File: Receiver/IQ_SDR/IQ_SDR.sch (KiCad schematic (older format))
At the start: 150 parts, among them CON1 SJ1-3523N, J1 ANT, J10 LO_I, J11 LO_Q, J12 GNDA, J13 I_IN, J14 Q_IN, J15 +5V, J16 4.3V, J17 I_OUT, J18 Q_OUT, J19 Conn_01x01_Male, J2 GND, J20 Conn_01x01_Male, J3 V_IN pin header, J4 GND, J5 V_IN, J6 FIL_O, J7 CLK1, J8 CLK2, J9 CLK0, P1 BNC, P2 SMA, Q1 MMBT2222A-TP, Q2 2N3904, Q3 2N3904, Q4 2N3904, Q5 2N3904, T1 Transformer_1P_SS, T2 Transformer_1P_1S, T3 Transformer_SP_1S, T4 Transformer_SP_1S, U1 FST3253 or TS3A5017, U2 Si5351A-B-GT, U3 TS5A23157, U4 LM4562 or LT6231, U5 74ALVC74D, Y1 CX3225

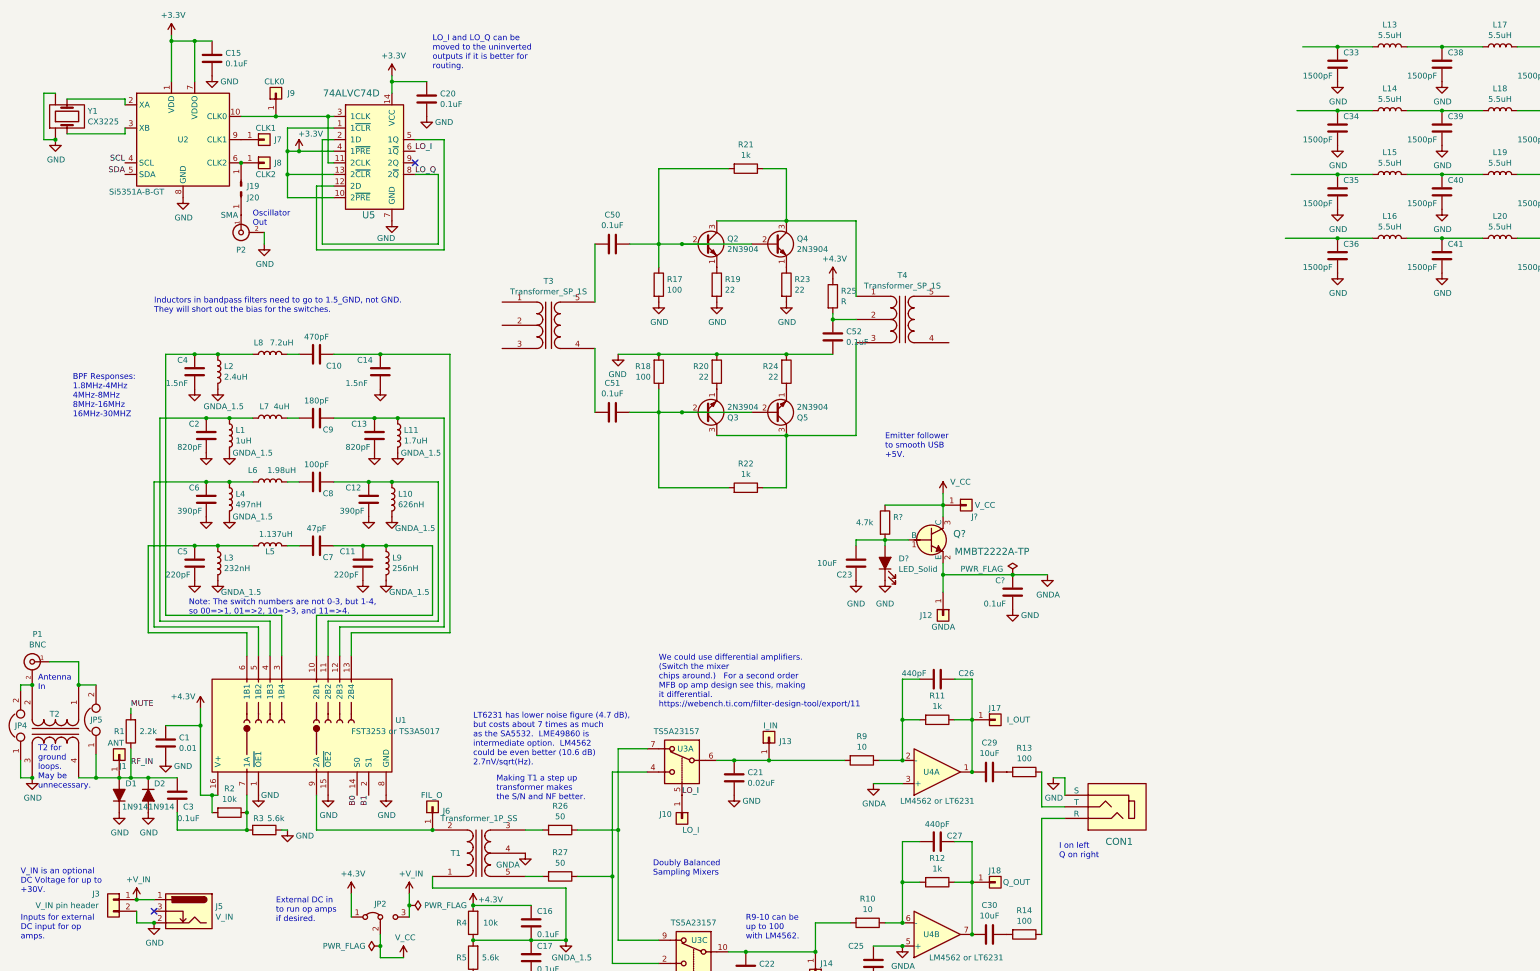
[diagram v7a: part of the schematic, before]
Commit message: added better voltage reference for the op amps
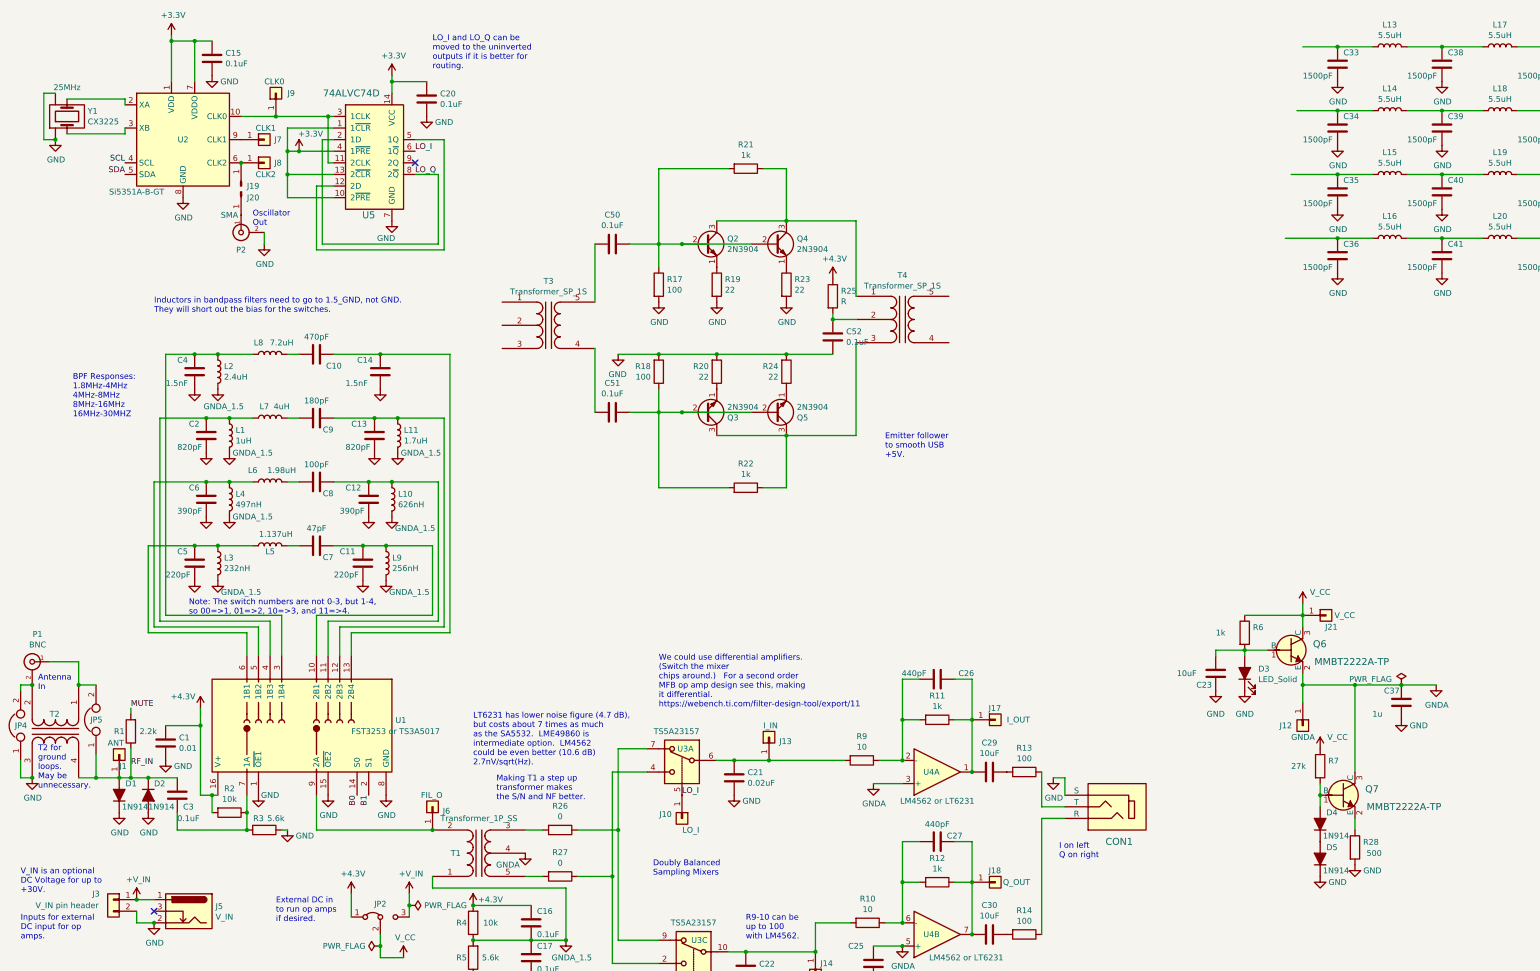
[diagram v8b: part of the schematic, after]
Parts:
- added D4, D5: 1N914, Diodes_SMD:D_SOD-323, symbol IQ_SDR-rescue:D_ALT-Device
- added Q7: MMBT2222A-TP, digikey-footprints:SOT-23-3, symbol IQ_SDR-rescue:MMBT2222A-TP-dk_Transistors-Bipolar-BJT-Single
- added R28: 500, Resistors_SMD:R_0805, symbol IQ_SDR-rescue:R-Device
- added R7: 27k, Resistors_SMD:R_0805, symbol IQ_SDR-rescue:R-Device
- C37: renamed from C?; value 0.1uF -> 1u
- R26, R27: value 50 -> 0
- R6: renamed from R?; value 4.7k -> 1k
- Y1: Frequency (none) -> 25MHz
- gave numbers to parts that had none: 3
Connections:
- wire segments 285 -> 290
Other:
- moved on the sheet: C23, C37, D3, J12, J21, Q6, R6
